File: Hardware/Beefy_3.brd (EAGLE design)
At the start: 22.9 x 15.9 mm, 21 parts, among them J1 USB-MINIB-5PIN, U1 3.3V, U2 FT232RL-BASICSSOP

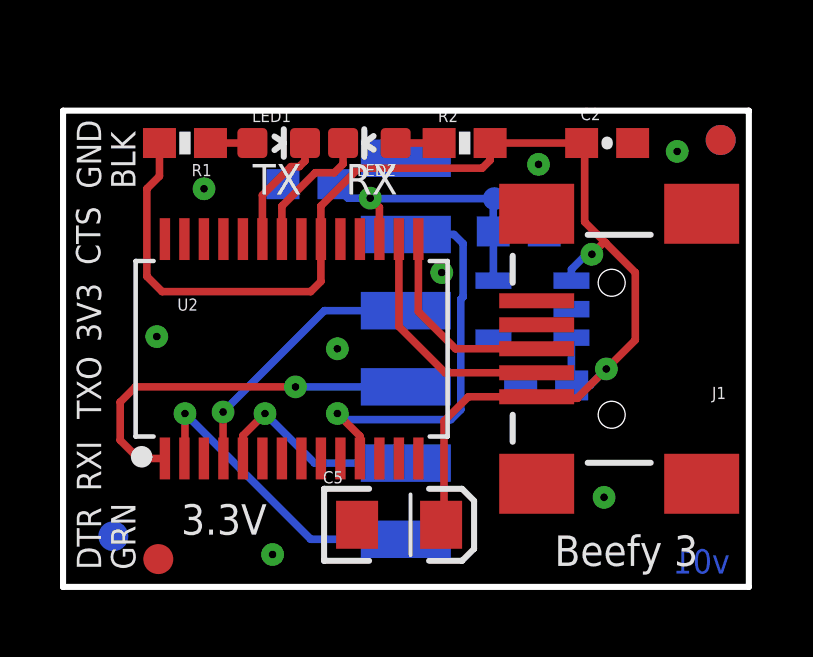
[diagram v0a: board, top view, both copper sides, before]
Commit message: Improved high-speed differential routing
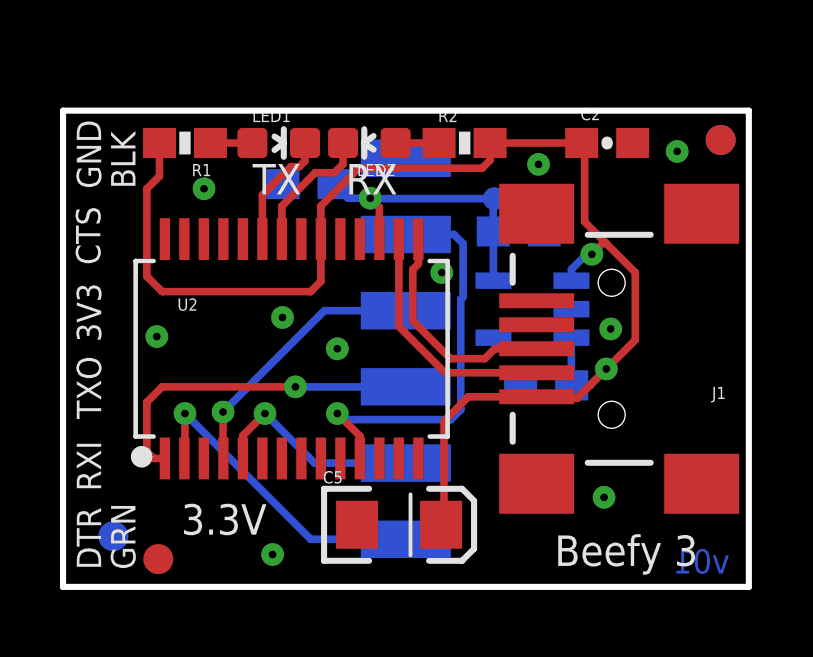
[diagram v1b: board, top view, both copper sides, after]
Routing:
- net TXO: track 12.7 -> 11.2 mm
- net USB_D+: track 6.87 -> 7.59 mm
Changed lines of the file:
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@@
 <setting verticaltext="up"/>
 </settings>
-<grid distance="0.001" unitdist="inch" unit="inch" style="lines" multiple="1" display="yes" altdistance="0.005" altunitdist="inch" altunit="inch"/>
+<grid distance="0.005" unitdist="inch" unit="inch" style="lines" multiple="1" display="yes" altdistance="0.0001" altunitdist="inch" altunit="inch"/>
 <layers>
 <layer number="1" name="Top" color="4" fill="1" visible="yes" active="yes"/>
@@
 <via x="15.8496" y="14.0843" extent="1-16" drill="0.254"/>
 <via x="9.144" y="7.9375" extent="1-16" drill="0.254"/>
+<via x="7.3152" y="8.9789" extent="1-16" drill="0.254"/>
+<via x="18.254978125" y="8.5979" extent="1-16" drill="0.254"/>
 </signal>
 <signal name="USB_D-">
@@
 </signal>
 <signal name="USB_D+">
-<wire x1="13.081" y1="7.9375" x2="15.788" y2="7.9375" width="0.254" layer="1"/>
-<wire x1="11.845" y1="9.1735" x2="11.845" y2="11.5935" width="0.254" layer="1"/>
-<wire x1="11.845" y1="9.1735" x2="13.081" y2="7.9375" width="0.254" layer="1"/>
+<wire x1="11.6586" y1="8.8646" x2="12.9159" y2="7.6073" width="0.254" layer="1"/>
 <contactref element="J1" pad="D+"/>
 <contactref element="U2" pad="15"/>
+<wire x1="15.788" y1="7.9375" x2="14.3891" y2="7.9375" width="0.254" layer="1"/>
+<wire x1="14.3891" y1="7.9375" x2="14.0589" y2="7.6073" width="0.254" layer="1"/>
+<wire x1="14.0589" y1="7.6073" x2="12.9159" y2="7.6073" width="0.254" layer="1"/>
+<wire x1="11.845" y1="11.5935" x2="11.845" y2="10.7655" width="0.254" layer="1"/>
+<wire x1="11.845" y1="10.7655" x2="11.6586" y2="10.5791" width="0.254" layer="1"/>
+<wire x1="11.6586" y1="10.5791" x2="11.6586" y2="8.8646" width="0.254" layer="1"/>
 </signal>
 <signal name="CTS">
@@
 <signal name="TXO">
 <contactref element="JP1" pad="4"/>
-<wire x1="2.513" y1="4.2815" x2="1.905" y2="4.8895" width="0.254" layer="1"/>
-<wire x1="1.905" y1="4.8895" x2="1.905" y2="6.1595" width="0.254" layer="1"/>
-<wire x1="1.905" y1="6.1595" x2="2.413" y2="6.6675" width="0.254" layer="1"/>
+<wire x1="3.021" y1="4.2815" x2="2.794" y2="4.5085" width="0.254" layer="1"/>
+<wire x1="2.794" y1="4.5085" x2="2.794" y2="6.1595" width="0.254" layer="1"/>
+<wire x1="2.794" y1="6.1595" x2="3.302" y2="6.6675" width="0.254" layer="1"/>
 <wire x1="7.747" y1="6.6675" x2="11.426" y2="6.6675" width="0.254" layer="16"/>
 <via x="7.747" y="6.6675" extent="1-16" drill="0.254"/>
 <contactref element="U2" pad="1"/>
-<wire x1="2.513" y1="4.2815" x2="3.395" y2="4.2815" width="0.254" layer="1"/>
-<wire x1="7.747" y1="6.6675" x2="2.413" y2="6.6675" width="0.254" layer="1"/>
+<wire x1="3.021" y1="4.2815" x2="3.395" y2="4.2815" width="0.254" layer="1"/>
+<wire x1="7.747" y1="6.6675" x2="3.302" y2="6.6675" width="0.254" layer="1"/>
 </signal>
 <signal name="RXI">

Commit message: Added PROD_IDs to library parts and updated them
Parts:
- JP1: device SparkFun:1X06-SMD-FEMALE-V2 -> SparkFun-Connectors:1X06-SMD-FEMALE-V2
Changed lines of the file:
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@@
 <attribute name="PROD_ID" value="DIO-00821" x="10.2108" y="14.7955" size="1.778" layer="27" rot="R90" display="off"/>
 </element>
-<element name="JP1" library="SparkFun" package="1X06-SMD-FEMALE-V2" value="" x="8.001" y="7.9375" rot="MR90"/>
+<element name="JP1" library="SparkFun-Connectors" package="1X06-SMD-FEMALE-V2" value="" x="8.001" y="7.9375" rot="MR90">
+<attribute name="PROD_ID" value="CONN-09668" x="8.001" y="7.9375" size="1.778" layer="28" rot="MR90" display="off"/>
+</element>
 <element name="JP3" library="SparkFun" package="FIDUCIAL-1X2" value="FIDUCIAL1X2" x="3.175" y="0.9271"/>
 <element name="JP4" library="SparkFun" package="FIDUCIAL-1X2" value="FIDUCIAL1X2" x="21.9202" y="14.8971"/>
@@
 <attribute name="PROD_ID" value="CONN-08193" x="18.288" y="7.9375" size="1.778" layer="27" rot="R180" display="off"/>
 </element>
-<element name="U2" library="SparkFun-DigitalIC" package="SSOP28DB" value="FT232RL-BASICSSOP" x="7.62" y="7.9375"/>
+<element name="U2" library="SparkFun-DigitalIC" package="SSOP28DB" value="FT232RL-BASICSSOP" x="7.62" y="7.9375">
+<attribute name="PROD_ID" value="IC-00870" x="7.62" y="7.9375" size="1.778" layer="27" display="off"/>
+</element>
 <element name="U1" library="SparkFun-PowerIC" package="SOT23-5" value="3.3V" x="15.6464" y="9.2583" rot="MR270">
 <attribute name="PROD_ID" value="VREG-12457" x="10.5664" y="13.0683" size="1.778" layer="28" rot="MR270" display="off"/>

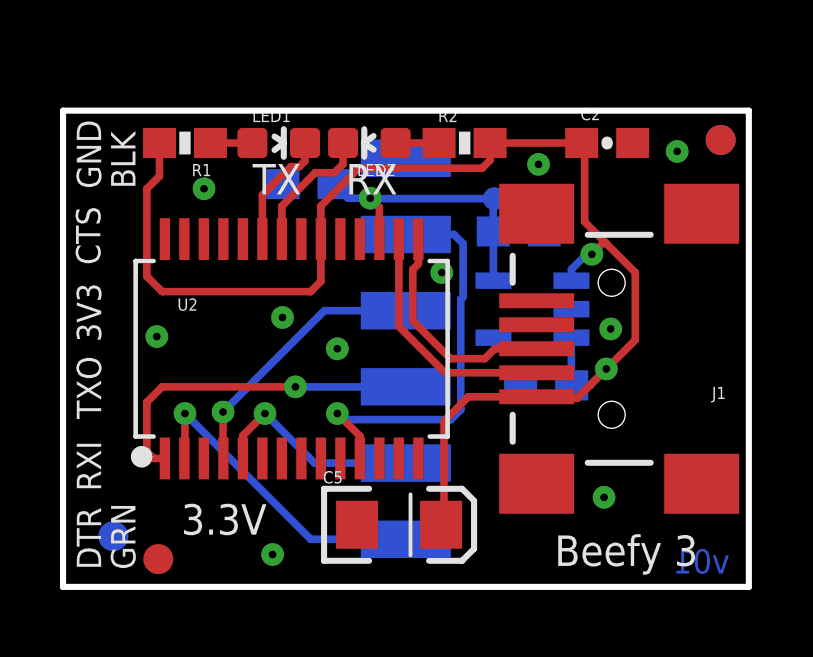
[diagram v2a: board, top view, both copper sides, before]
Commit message: First pass at using micro B & FT231X
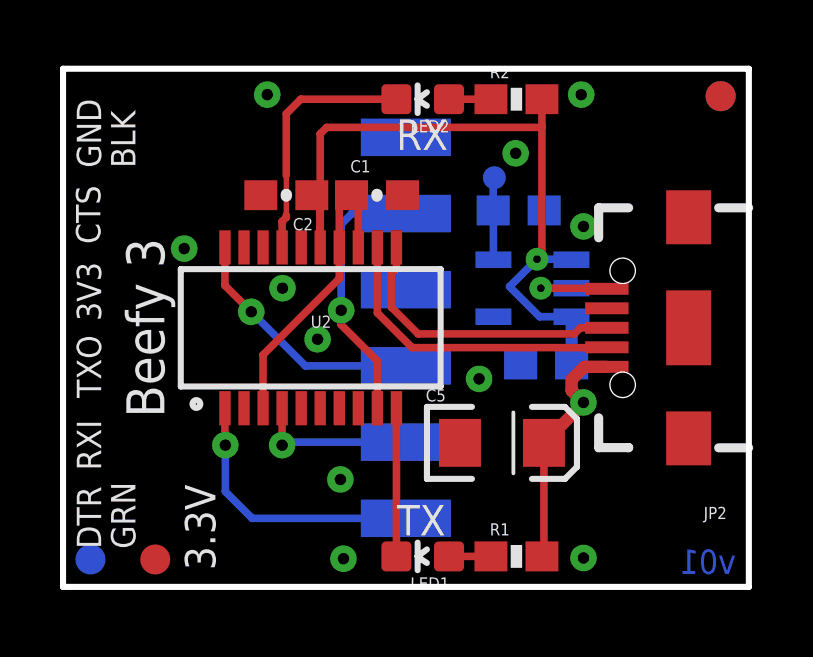
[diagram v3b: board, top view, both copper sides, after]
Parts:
- removed J1: USB-MINIB-5PIN, SparkFun-Connectors:USB-MINIB
- added JP2: (no value), SparkFun-Connectors:USB-B-MICRO-SMD_V03
- U2: value FT232RL-BASICSSOP -> FTS31XS-U; device SparkFun-DigitalIC:SSOP28DB -> SparkFun-DigitalIC:SSOP20_L
- moved R1 17.7 mm to (15.1, 1.02), turned to 0 degrees
- moved LED1 14.6 mm to (12.0, 1.02), turned to 90 degrees
- moved C2 10.8 mm to (7.44, 13.1), turned to 180 degrees
- moved C5 4.38 mm to (14.6, 4.80)
- moved C1 2.32 mm to (10.5, 13.1), flipped to the top
- moved LED2 2.30 mm to (12.0, 16.3)
- moved R2 2.26 mm to (15.1, 16.3)
- moved JP4 1.46 mm to (21.9, 16.4)
- moved JP6 1.46 mm to (21.9, 16.4)
- moved JP5 1.09 mm to (0.91, 0.91)
- moved U2 0.94 mm to (8.26, 8.64)
- moved C3 0.70 mm to (16.1, 7.42)
- moved C4 0.70 mm to (15.2, 12.5)
- moved JP1 0.70 mm to (8.00, 8.64)
- moved LOGO1 0.70 mm to (18.1, 13.7)
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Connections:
- removed net CTS: JP1.2, U2.11
- removed net DTR: JP1.6, U2.2
- new net !CTS: JP1.2, U2.9
- new net !DTR: JP1.6, U2.1
- new net 3V3LC: C1.1, U2.13, U2.14, U2.3
- net 3.3V: no longer U2.4
- net 3V3: no longer C1.1, U2.17
- net 5V: now also JP2.VBUS1, U2.15; no longer J1.VBUS, U2.20
- net GND: now also JP2.GND1, U2.16, U2.6; no longer J1.GND, U2.18, U2.21, U2.25, U2.26, U2.7
- net RXI: now also U2.4; no longer U2.5
- net RXLED: now also U2.17; no longer U2.22
- net TXLED: now also U2.10; no longer U2.23
- net TXO: now also U2.20; no longer U2.1
- net USB_D+: now also JP2.D+1, U2.11; no longer J1.D+, U2.15
- net USB_D-: now also JP2.D-1, U2.12; no longer J1.D-, U2.16
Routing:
- net CTS: track 13.7 -> 0.00 mm, vias 1 -> 0
- net 5V: track 46.6 -> 34.5 mm
- net DTR: track 10.6 -> 0.00 mm, vias 1 -> 0
- net 3V3LC: track 0.00 -> 10.2 mm
- net !DTR: track 0.00 -> 9.17 mm, vias 0 -> 1
- net 3.3V: track 9.04 -> 0.00 mm, vias 1 -> 0
- net !CTS: track 0.00 -> 8.94 mm, vias 0 -> 1
- net 3V3: track 10.1 -> 2.75 mm, vias 1 -> 0
- net RXLED: track 4.42 -> 8.39 mm
- net GND: track 0.00 -> 3.24 mm, vias 10 -> 12
- net TXO: track 11.2 -> 8.41 mm
- net USB_D-: track 8.15 -> 10.3 mm
- net USB_D+: track 7.59 -> 9.70 mm
- net RXI: track 7.18 -> 5.40 mm
- net TXLED: track 3.95 -> 4.94 mm
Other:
- board size 22.9 x 15.9 mm -> 22.9 x 17.3 mm

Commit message: New layout
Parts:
- removed LED1: RED, SparkFun-LED:LED-0603
- removed LED2: GREEN, SparkFun-LED:LED-0603
- removed TP1: TEST-POINT3, SparkFun-Passives:PAD.03X.03
- added D1: GREEN, SparkFun-LED:LED-0603
- added D2: RED, SparkFun-LED:LED-0603
- C1, C2: value 0.1uF -> 1.0uF
- C3: value 1.0uF -> 0.1uF
- C4: value 1.0uF -> 10uF; device SparkFun-Capacitors:0603-CAP -> SparkFun-Capacitors:EIA3216
- C5: value 10uF -> 0.1uF; device SparkFun-Capacitors:EIA3216 -> SparkFun-Capacitors:0603-CAP
- JP1: device SparkFun-Connectors:1X06-SMD-FEMALE-V2 -> SparkFun-Connectors:USB-B-MICRO-SMD_V03
- JP2: device SparkFun-Connectors:USB-B-MICRO-SMD_V03 -> SparkFun-Connectors:1X06-SMD-FEMALE-V2
- moved JP4 26.1 mm to (0.91, 0.91), flipped to the bottom
- moved JP5 26.1 mm to (21.9, 16.4), flipped to the top
- moved R2 15.5 mm to (6.15, 3.56), turned to 180 degrees
- moved R1 15.2 mm to (6.15, 13.3), turned to 180 degrees
- moved JP1 12.9 mm to (20.9, 8.64), flipped to the top, turned to 180 degrees
- moved JP2 12.9 mm to (8.00, 8.64), flipped to the bottom, turned to 90 degrees
- moved C4 11.3 mm to (19.7, 2.21), flipped to the top
- moved U1 10.8 mm to (4.93, 8.64), flipped to the top
- moved C5 8.84 mm to (13.3, 13.5), turned to 90 degrees
- moved C1 8.46 mm to (2.34, 10.7), turned to 90 degrees
- moved C3 7.33 mm to (12.1, 13.5), flipped to the top, turned to 90 degrees
- moved U2 3.17 mm to (11.4, 8.64)
- moved C2 2.52 mm to (5.36, 11.6)
- renumbered FRAME2 to FRAME1, U$2 to LOGO2
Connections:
- removed net 3.3V: JP1.3
- net !CTS: now also JP2.2; no longer JP1.2
- net !DTR: now also JP2.6; no longer JP1.6
- net 3V3: now also C2.1, JP2.3; no longer C4.1, TP1.P$1
- net 3V3LC: now also C5.1; no longer C1.1
- net 5V: now also C1.1, C4.A, JP1.VBUS1; no longer C2.1, C5.A, JP2.VBUS1
- net GND: now also C4.C, C5.2, JP1.GND1, JP2.1; no longer C4.2, C5.C, JP1.1, JP2.GND1
- net N$1: now also D2.A, R2.1; no longer LED1.A, R1.1
- net N$2: now also D1.A, R1.1; no longer LED2.A, R2.1
- net RXI: now also JP2.5; no longer JP1.5
- net RXLED: now also D1.C; no longer LED2.C
- net TXLED: now also D2.C; no longer LED1.C
- net TXO: now also JP2.4; no longer JP1.4
- net USB_D+: now also JP1.D+1; no longer JP2.D+1
- net USB_D-: now also JP1.D-1; no longer JP2.D-1
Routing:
- net 5V: track 34.5 -> 44.2 mm, vias 2 -> 7
- net RXLED: track 8.39 -> 2.08 mm
- net 3V3: track 2.75 -> 7.50 mm, vias 0 -> 1
- net USB_D+: track 9.70 -> 5.56 mm
- net USB_D-: track 10.3 -> 6.29 mm
- net GND: track 3.24 -> 0.00 mm
- net !DTR: track 9.17 -> 6.27 mm
- net TXO: track 8.41 -> 6.71 mm
- net RXI: track 5.40 -> 4.40 mm
- net TXLED: track 4.94 -> 5.73 mm, vias 0 -> 2
- net 3V3LC: track 10.2 -> 9.42 mm
- added copper zone on layer 1, net 5V
- added copper zone on layer 16, net 5V
